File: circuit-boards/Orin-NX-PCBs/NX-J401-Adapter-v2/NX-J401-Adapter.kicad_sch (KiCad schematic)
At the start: 19 parts, among them J10 CAN-PT-FD2, J11 CAN-FD1, J12 CAN-PT-FD1, J13 Power, J2 18V_OUT, J4 FAN, J7 CAN-FD2, J8 CAN-FD1, J9 CAN-FD2

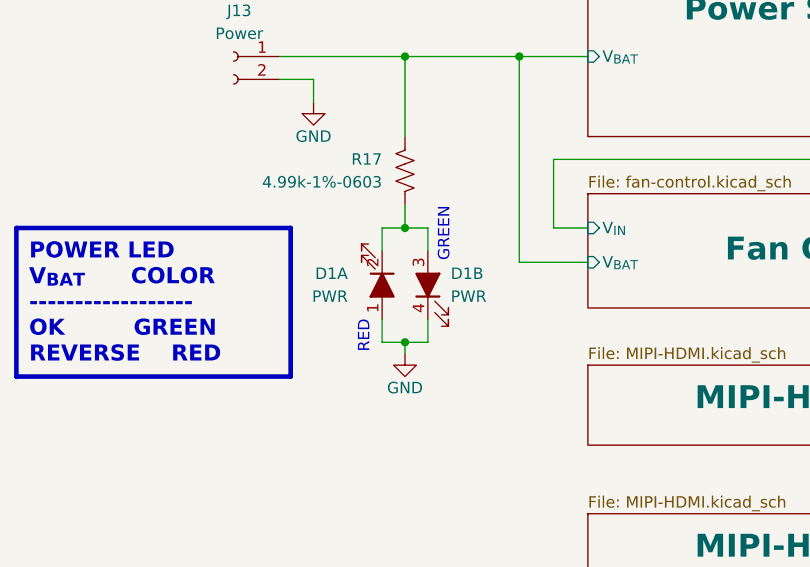
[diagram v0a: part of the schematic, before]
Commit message: Modified to expand M.2 adapter space, temp sensor connector and pwr LED
Signed-off-by: Scott <sgberman1@gmail.com>
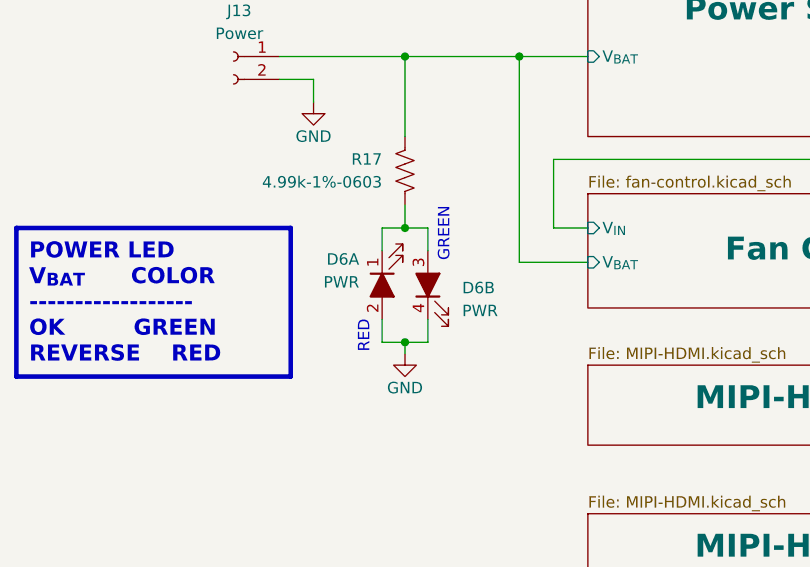
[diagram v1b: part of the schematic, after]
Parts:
- removed D1: PWR, NX-J401-Adapter:LED_SunLED_XZMDKVG55W-8, symbol NX-IndicatorBoard:SunLED-Dual-LED
- added D6: PWR, NX-J401-Adapter:LED-Dialight-5913001858F, symbol NX-AdapterBoard:Dialight-Dual-LED
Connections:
- net GND: now also D6.2 (RedA), D6.4 (Green-K)
- net at R17.1: now also D6.1 (Red-K), D6.3 (Green-A)
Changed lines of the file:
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@@
+    )
+  )
+  (symbol (lib_id "NX-AdapterBoard:Dialight-Dual-LED") (at 167.64 83.82 90) (unit 2)
+    (in_bom yes) (on_board yes) (dnp no) (fields_autoplaced)
+    (property "Reference" "D6" (at 171.45 84.1375 90)
+      (effects (font (size 1.27 1.27)) (justify right))
+    )
+    (property "Value" "PWR" (at 171.45 86.6775 90)
+      (effects (font (size 1.27 1.27)) (justify right))
+    )
+    (property "Footprint" "NX-J401-Adapter:LED-Dialight-5913001858F" (at 167.64 83.82 0)
+      (effects (font (size 1.27 1.27)) hide)
+    )
+    (property "Datasheet" "Components/Dialight-C18340B.pdf" (at 167.64 83.82 0)
+      (effects (font (size 1.27 1.27)) hide)
+    )
+    (property "MFG" "Dialight" (at 167.64 83.82 0)
+      (effects (font (size 1.27 1.27)) hide)
+    )
+    (property "MFG P/N" "5913001858F" (at 167.64 83.82 0)
+      (effects (font (size 1.27 1.27)) hide)
+    )
+    (property "DIST" "Digikey" (at 167.64 83.82 0)
+      (effects (font (size 1.27 1.27)) hide)
+    )
+    (property "DIST P/N" "350-5913001858FCT-ND" (at 167.64 83.82 0)
+      (effects (font (size 1.27 1.27)) hide)
+    )
+    (pin "1")
+    (pin "2")
+    (pin "3")
+    (pin "4")
+    (instances
+      (project "NX-J401-Adapter"
+        (path "/cc31ce4b-09ab-4aea-a1d3-ed84696ba658"
+          (reference "D6") (unit 2)
+        )
+      )
     )
   )
@@
     )
   )
-  (symbol (lib_name "SunLED-Dual-LED_1") (lib_id "NX-IndicatorBoard:SunLED-Dual-LED") (at 167.64 83.82 90) (unit 2)
-    (in_bom yes) (on_board yes) (dnp no)
-    (property "Reference" "D1" (at 170.18 82.55 90)
-      (effects (font (size 1.27 1.27)) (justify right))
-    )
-    (property "Value" "PWR" (at 170.18 85.09 90)
-      (effects (font (size 1.27 1.27)) (justify right))
-    )
-    (property "Footprint" "NX-J401-Adapter:LED_SunLED_XZMDKVG55W-8" (at 167.64 83.82 0)
-      (effects (font (size 1.27 1.27)) hide)
-    )
-    (property "Datasheet" "Components/SunLED-XZMDKVG55W-8.pdf" (at 167.64 83.82 0)
-      (effects (font (size 1.27 1.27)) hide)
-    )
-    (property "MFG" "SunLED" (at 167.64 83.82 0)
-      (effects (font (size 1.27 1.27)) hide)
-    )
-    (property "MFG P/N" "XZMDKVG55W-8" (at 167.64 83.82 0)
-      (effects (font (size 1.27 1.27)) hide)
-    )
-    (property "DIST" "Digikey" (at 167.64 83.82 0)
-      (effects (font (size 1.27 1.27)) hide)
-    )
-    (property "DIST P/N" "1497-1183-1-ND" (at 167.64 83.82 0)
-      (effects (font (size 1.27 1.27)) hide)
-    )
-    (pin "1")
-    (pin "2")
-    (pin "3")
-    (pin "4")
-    (instances
-      (project "NX-IndicatorBoard"
-        (path "/b2b9b2ba-ad3f-4e65-98f2-b291a62e1006/64dd458f-3f8e-470e-9441-6a9cd5c8d120"
-          (reference "D1") (unit 2)
-        )
-      )
-      (project "NX-J401-Adapter"
-        (path "/cc31ce4b-09ab-4aea-a1d3-ed84696ba658"
-          (reference "D6") (unit 2)
-        )
-      )
-    )
-  )
   (symbol (lib_id "Graphic:SYM_Arrow_Large") (at 288.29 104.14 0) (unit 1)
     (in_bom no) (on_board no) (dnp no)
@@
     )
   )
-  (symbol (lib_id "NX-IndicatorBoard:SunLED-Dual-LED") (at 162.56 83.82 270) (unit 1)
-    (in_bom yes) (on_board yes) (dnp no)
-    (property "Reference" "D1" (at 158.75 82.55 90)
-      (effects (font (size 1.27 1.27)) (justify right))
-    )
-    (property "Value" "PWR" (at 158.75 85.09 90)
-      (effects (font (size 1.27 1.27)) (justify right))
-    )
-    (property "Footprint" "NX-J401-Adapter:LED_SunLED_XZMDKVG55W-8" (at 162.56 83.82 0)
-      (effects (font (size 1.27 1.27)) hide)
-    )
-    (property "Datasheet" "Components/SunLED-XZMDKVG55W-8.pdf" (at 162.56 83.82 0)
-      (effects (font (size 1.27 1.27)) hide)
-    )
-    (property "MFG" "SunLED" (at 162.56 83.82 0)
-      (effects (font (size 1.27 1.27)) hide)
-    )
-    (property "MFG P/N" "XZMDKVG55W-8" (at 162.56 83.82 0)
-      (effects (font (size 1.27 1.27)) hide)
-    )
-    (property "DIST" "Digikey" (at 162.56 83.82 0)
-      (effects (font (size 1.27 1.27)) hide)
-    )
-    (property "DIST P/N" "1497-1183-1-ND" (at 162.56 83.82 0)
-      (effects (font (size 1.27 1.27)) hide)
-    )
-    (pin "1")
-    (pin "2")
-    (pin "3")
-    (pin "4")
-    (instances
-      (project "NX-IndicatorBoard"
-        (path "/b2b9b2ba-ad3f-4e65-98f2-b291a62e1006/64dd458f-3f8e-470e-9441-6a9cd5c8d120"
-          (reference "D1") (unit 1)
-        )
-      )
-      (project "NX-J401-Adapter"
-        (path "/cc31ce4b-09ab-4aea-a1d3-ed84696ba658"
-          (reference "D6") (unit 1)
-        )
-      )
-    )
-  )
   (symbol (lib_id "power:GND") (at 256.54 86.36 0) (mirror y) (unit 1)
     (in_bom yes) (on_board yes) (dnp no)
@@
         )
       )
+    )
+  )
+  (symbol (lib_id "NX-AdapterBoard:Dialight-Dual-LED") (at 162.56 83.82 90) (mirror x) (unit 1)
+    (in_bom yes) (on_board yes) (dnp no)
+    (property "Reference" "D6" (at 160.02 80.9625 90)
+      (effects (font (size 1.27 1.27)) (justify left))
+    )
+    (property "Value" "PWR" (at 160.02 83.5025 90)
+      (effects (font (size 1.27 1.27)) (justify left))
+    )
+    (property "Footprint" "NX-J401-Adapter:LED-Dialight-5913001858F" (at 162.56 83.82 0)
+      (effects (font (size 1.27 1.27)) hide)
+    )
+    (property "Datasheet" "Components/Dialight-C18340B.pdf" (at 162.56 83.82 0)
+      (effects (font (size 1.27 1.27)) hide)
+    )
+    (property "MFG" "Dialight" (at 162.56 83.82 0)
+      (effects (font (size 1.27 1.27)) hide)
+    )
+    (property "MFG P/N" "5913001858F" (at 162.56 83.82 0)
+      (effects (font (size 1.27 1.27)) hide)
+    )
+    (property "DIST" "Digikey" (at 162.56 83.82 0)
+      (effects (font (size 1.27 1.27)) hide)
+    )
+    (property "DIST P/N" "350-5913001858FCT-ND" (at 162.56 83.82 0)
+      (effects (font (size 1.27 1.27)) hide)
+    )
+    (pin "1")
+    (pin "2")
+    (pin "3")
+    (pin "4")
+    (instances
+      (project "NX-J401-Adapter"
+        (path "/cc31ce4b-09ab-4aea-a1d3-ed84696ba658"
+          (reference "D6") (unit 1)
+        )
+      )

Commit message: Modified sys dwg rio ethernet, added comment to nx adapter
Signed-off-by: Scott Berman <sgberman1@gmail.com>
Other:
- note added: "Revision Notes 1. CAN SUR connectors have pin 1 side swapped"
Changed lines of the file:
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@@
     (effects (font (face "FreeMono") (size 1.778 1.778) (thickness 0.3556) bold (color 0 0 0 1)) (justify left top))
+  )
+  (text "Revision Notes\n1. CAN SUR connectors have pin 1 side swapped"
+    (at 290.83 24.13 0)
+    (effects (font (size 1.905 1.905) (thickness 0.381) bold (color 255 0 0 1)) (justify left bottom))
   )
   (text "FFC: 36 pin" (at 360.68 80.01 0)
@@
       )
       (project "NX-J401-Adapter"
-        (path "/cc31ce4b-09ab-4aea-a1d3-ed84696ba658/584f7d71-5922-4ce5-8f88-d664ca9e2a8c"
-          (reference "R7") (unit 1)
-        )
-        (path "/cc31ce4b-09ab-4aea-a1d3-ed84696ba658/31806f24-7fa6-46e2-ae93-f7306b662757"
-          (reference "R5") (unit 1)
-        )
         (path "/cc31ce4b-09ab-4aea-a1d3-ed84696ba658"
           (reference "R11") (unit 1)
